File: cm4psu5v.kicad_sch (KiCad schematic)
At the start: 26 parts, among them U13 AP64501SP-13

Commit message: respin
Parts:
- renumbered C46 to C48, C47 to C49, C48 to C50, C49 to C51, C50 to C52, C51 to C53, C52 to C54, C53 to C55, C54 to C56, C55 to C57, C56 to C58, C57 to C59, C58 to C60, C59 to C61, C60 to C62, C61 to C63, D10 to D9, R39 to R42, R40 to R43, R41 to R44, R42 to R45, R43 to R46, U13 to U14
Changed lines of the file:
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@@
   (symbol (lib_id "power:GND") (at 152.4 148.59 0) (unit 1)
     (in_bom yes) (on_board yes)
-    (property "Reference" "#PWR043" (id 0) (at 152.4 154.94 0)
+    (property "Reference" "#PWR044" (id 0) (at 152.4 154.94 0)
       (effects (font (size 1.27 1.27)) hide)
     )
@@
   (symbol (lib_id "Device:C_Small") (at 259.08 111.76 0) (unit 1)
     (in_bom yes) (on_board yes)
-    (property "Reference" "C58" (id 0) (at 261.62 110.49 0)
+    (property "Reference" "C60" (id 0) (at 261.62 110.49 0)
       (effects (font (size 1.27 1.27)) (justify left))
     )
@@
   (symbol (lib_id "Device:R_Small") (at 226.06 137.16 0) (unit 1)
     (in_bom yes) (on_board yes)
-    (property "Reference" "R42" (id 0) (at 227.33 135.89 0)
+    (property "Reference" "R45" (id 0) (at 227.33 135.89 0)
       (effects (font (size 1.27 1.27)) (justify left))
     )
@@
   (symbol (lib_id "Device:R_Small") (at 219.71 118.11 0) (unit 1)
     (in_bom yes) (on_board yes)
-    (property "Reference" "R41" (id 0) (at 220.98 116.84 0)
+    (property "Reference" "R44" (id 0) (at 220.98 116.84 0)
       (effects (font (size 1.27 1.27)) (justify left))
     )
@@
   (symbol (lib_id "Device:C_Small") (at 232.41 118.11 0) (unit 1)
     (in_bom no) (on_board no)
-    (property "Reference" "C56" (id 0) (at 234.95 116.84 0)
+    (property "Reference" "C58" (id 0) (at 234.95 116.84 0)
       (effects (font (size 1.27 1.27)) (justify left))
     )
@@
   (symbol (lib_id "Device:C_Small") (at 213.36 140.97 0) (unit 1)
     (in_bom yes) (on_board yes)
-    (property "Reference" "C55" (id 0) (at 215.9 139.7 0)
+    (property "Reference" "C57" (id 0) (at 215.9 139.7 0)
       (effects (font (size 1.27 1.27)) (justify left))
     )
@@
   (symbol (lib_id "Device:R_Small") (at 306.705 112.395 0) (unit 1)
     (in_bom yes) (on_board yes)
-    (property "Reference" "R43" (id 0) (at 309.88 111.125 0))
+    (property "Reference" "R46" (id 0) (at 309.88 111.125 0))
     (property "Value" "1k" (id 1) (at 309.88 113.665 0))
     (property "Footprint" "Resistor_SMD:R_0402_1005Metric" (id 2) (at 306.705 112.395 0)
@@
   (symbol (lib_id "power:GND") (at 290.83 148.59 0) (unit 1)
     (in_bom yes) (on_board yes)
-    (property "Reference" "#PWR047" (id 0) (at 290.83 154.94 0)
+    (property "Reference" "#PWR048" (id 0) (at 290.83 154.94 0)
       (effects (font (size 1.27 1.27)) hide)
     )
@@
   (symbol (lib_id "Regulator_Switching_Diodes:AP64501SP-13") (at 182.88 124.46 0) (unit 1)
     (in_bom yes) (on_board yes)
-    (property "Reference" "U13" (id 0) (at 182.245 114.3 0))
+    (property "Reference" "U14" (id 0) (at 182.245 114.3 0))
     (property "Value" "AP64501SP-13" (id 1) (at 182.88 116.84 0))
     (property "Footprint" "Regulator_Switching_Diodes:SOIC-8-1EP_3.9x4.9mm_P1.27mm_EP2.95x4.9mm_Mask2.71x3.4mm_ThermalVias" (id 2) (at 182.88 149.86 0)
@@
   (symbol (lib_id "Device:C_Small") (at 248.92 111.76 0) (unit 1)
     (in_bom yes) (on_board yes)
-    (property "Reference" "C57" (id 0) (at 251.46 110.49 0)
+    (property "Reference" "C59" (id 0) (at 251.46 110.49 0)
       (effects (font (size 1.27 1.27)) (justify left))
     )
@@
   (symbol (lib_id "power:GND") (at 279.4 148.59 0) (unit 1)
     (in_bom yes) (on_board yes)
-    (property "Reference" "#PWR046" (id 0) (at 279.4 154.94 0)
+    (property "Reference" "#PWR047" (id 0) (at 279.4 154.94 0)
       (effects (font (size 1.27 1.27)) hide)
     )
@@
   (symbol (lib_id "Device:C_Small") (at 163.83 114.3 0) (unit 1)
     (in_bom yes) (on_board yes)
-    (property "Reference" "C52" (id 0) (at 166.37 113.03 0)
+    (property "Reference" "C54" (id 0) (at 166.37 113.03 0)
       (effects (font (size 1.27 1.27)) (justify left))
     )
@@
   (symbol (lib_id "Device:R_Small") (at 173.99 106.68 270) (unit 1)
     (in_bom yes) (on_board yes)
-    (property "Reference" "R39" (id 0) (at 172.72 104.14 90)
+    (property "Reference" "R42" (id 0) (at 172.72 104.14 90)
       (effects (font (size 1.27 1.27)) (justify left))
     )
@@
   (symbol (lib_id "Device:R_Small") (at 213.36 133.35 0) (unit 1)
     (in_bom yes) (on_board yes)
-    (property "Reference" "R40" (id 0) (at 215.9 132.08 0)
+    (property "Reference" "R43" (id 0) (at 215.9 132.08 0)
       (effects (font (size 1.27 1.27)) (justify left))
     )
@@
   (symbol (lib_id "Device:C_Small") (at 279.4 111.76 0) (unit 1)
     (in_bom yes) (on_board yes)
-    (property "Reference" "C60" (id 0) (at 281.94 110.49 0)
+    (property "Reference" "C62" (id 0) (at 281.94 110.49 0)
       (effects (font (size 1.27 1.27)) (justify left))
     )
@@
   (symbol (lib_id "Device:C_Small") (at 172.72 137.16 0) (unit 1)
     (in_bom yes) (on_board yes)
-    (property "Reference" "C53" (id 0) (at 175.26 135.89 0)
+    (property "Reference" "C55" (id 0) (at 175.26 135.89 0)
       (effects (font (size 1.27 1.27)) (justify left))
     )
@@
   (symbol (lib_id "power:GND") (at 226.06 148.59 0) (unit 1)
     (in_bom yes) (on_board yes)
-    (property "Reference" "#PWR044" (id 0) (at 226.06 154.94 0)
+    (property "Reference" "#PWR045" (id 0) (at 226.06 154.94 0)
       (effects (font (size 1.27 1.27)) hide)
     )
@@
   (symbol (lib_id "Device:C_Small") (at 152.4 128.27 0) (unit 1)
     (in_bom yes) (on_board yes)
-    (property "Reference" "C51" (id 0) (at 154.94 127 0)
+    (property "Reference" "C53" (id 0) (at 154.94 127 0)
       (effects (font (size 1.27 1.27)) (justify left))
     )
@@
   (symbol (lib_id "Device:C_Small") (at 91.44 128.27 0) (unit 1)
     (in_bom yes) (on_board yes)
-    (property "Reference" "C47" (id 0) (at 93.98 127 0)
+    (property "Reference" "C49" (id 0) (at 93.98 127 0)
       (effects (font (size 1.27 1.27)) (justify left))
     )
@@
   (symbol (lib_id "Device:C_Small") (at 269.24 111.76 0) (unit 1)
     (in_bom yes) (on_board yes)
-    (property "Reference" "C59" (id 0) (at 271.78 110.49 0)
+    (property "Reference" "C61" (id 0) (at 271.78 110.49 0)
       (effects (font (size 1.27 1.27)) (justify left))
     )
@@
   (symbol (lib_id "power:GND") (at 306.705 148.59 0) (unit 1)
     (in_bom yes) (on_board yes)
-    (property "Reference" "#PWR048" (id 0) (at 306.705 154.94 0)
+    (property "Reference" "#PWR049" (id 0) (at 306.705 154.94 0)
       (effects (font (size 1.27 1.27)) hide)
     )
@@
   (symbol (lib_id "Device:C_Small") (at 76.2 128.27 0) (unit 1)
     (in_bom yes) (on_board yes)
-    (property "Reference" "C46" (id 0) (at 78.74 127 0)
+    (property "Reference" "C48" (id 0) (at 78.74 127 0)
       (effects (font (size 1.27 1.27)) (justify left))
     )
@@
   (symbol (lib_id "power:GND") (at 251.46 142.24 0) (unit 1)
     (in_bom yes) (on_board yes)
-    (property "Reference" "#PWR045" (id 0) (at 251.46 148.59 0)
+    (property "Reference" "#PWR046" (id 0) (at 251.46 148.59 0)
       (effects (font (size 1.27 1.27)) hide)
     )
@@
   (symbol (lib_id "Capacitor_Tantalum_SMD_MyOwn:CP_EIA-7343-31_Kemet-D") (at 290.83 111.76 0) (unit 1)
     (in_bom yes) (on_board yes)
-    (property "Reference" "C61" (id 0) (at 293.37 110.49 0)
+    (property "Reference" "C63" (id 0) (at 293.37 110.49 0)
       (effects (font (size 1.27 1.27)) (justify left))
     )
@@
   (symbol (lib_id "Device:C_Small") (at 121.92 128.27 0) (unit 1)
     (in_bom yes) (on_board yes)
-    (property "Reference" "C49" (id 0) (at 124.46 127 0)
+    (property "Reference" "C51" (id 0) (at 124.46 127 0)
       (effects (font (size 1.27 1.27)) (justify left))
     )
@@
   (symbol (lib_id "Device:C_Small") (at 106.68 128.27 0) (unit 1)
     (in_bom yes) (on_board yes)
-    (property "Reference" "C48" (id 0) (at 109.22 127 0)
+    (property "Reference" "C50" (id 0) (at 109.22 127 0)
       (effects (font (size 1.27 1.27)) (justify left))
     )
@@
   (symbol (lib_id "Device:C_Small") (at 137.16 128.27 0) (unit 1)
     (in_bom yes) (on_board yes)
-    (property "Reference" "C50" (id 0) (at 139.7 127 0)
+    (property "Reference" "C52" (id 0) (at 139.7 127 0)
       (effects (font (size 1.27 1.27)) (justify left))
     )
@@
   (symbol (lib_id "Device:C_Small") (at 201.93 137.16 0) (unit 1)
     (in_bom yes) (on_board yes)
-    (property "Reference" "C54" (id 0) (at 204.47 135.89 0)
+    (property "Reference" "C56" (id 0) (at 204.47 135.89 0)
       (effects (font (size 1.27 1.27)) (justify left))
     )
@@
   (symbol (lib_id "LED_SMD_LiteOn:LED Green") (at 306.705 121.285 270) (unit 1)
     (in_bom yes) (on_board yes)
-    (property "Reference" "D10" (id 0) (at 309.88 120.65 90))
+    (property "Reference" "D9" (id 0) (at 309.88 120.65 90))
     (property "Value" "LED Green" (id 1) (at 313.69 122.555 90))
     (property "Footprint" "LED_SMD_LiteOn:LED_0603_1608Metric_green" (id 2) (at 296.545 121.285 0)

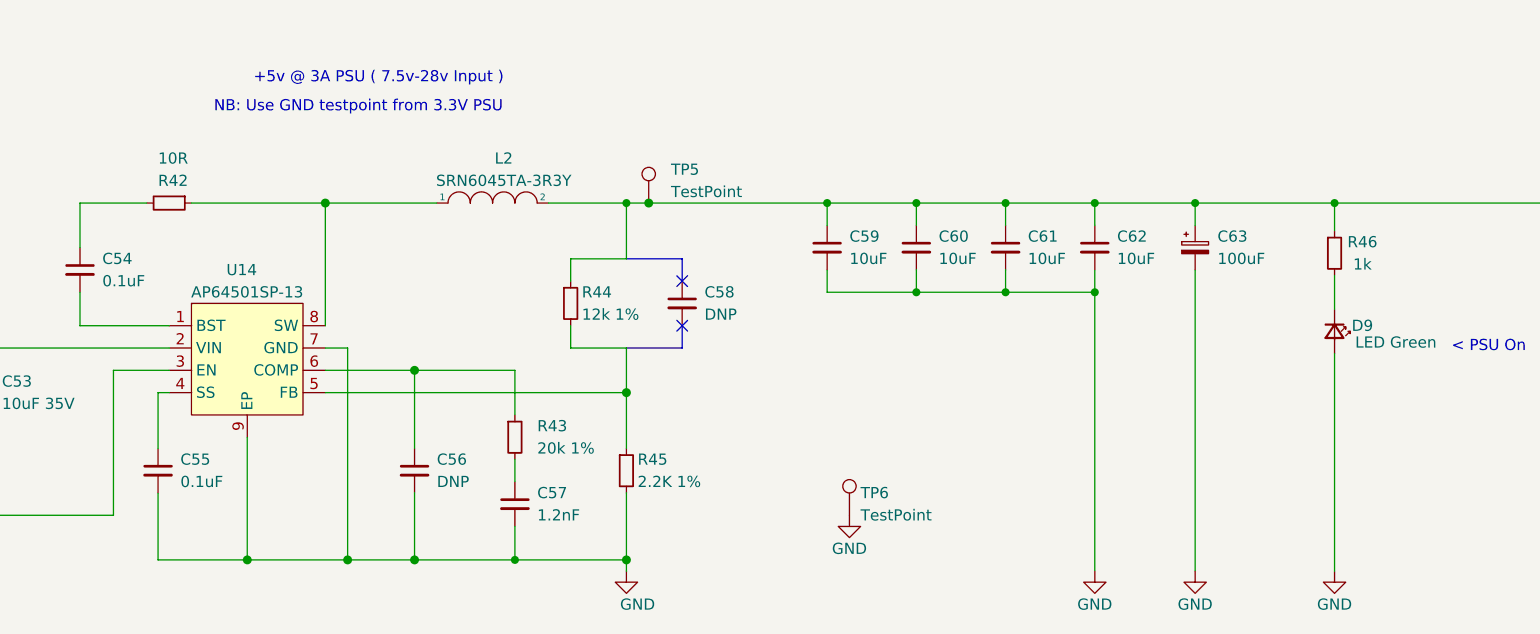
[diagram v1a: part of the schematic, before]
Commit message: fixed I2C ping indicator
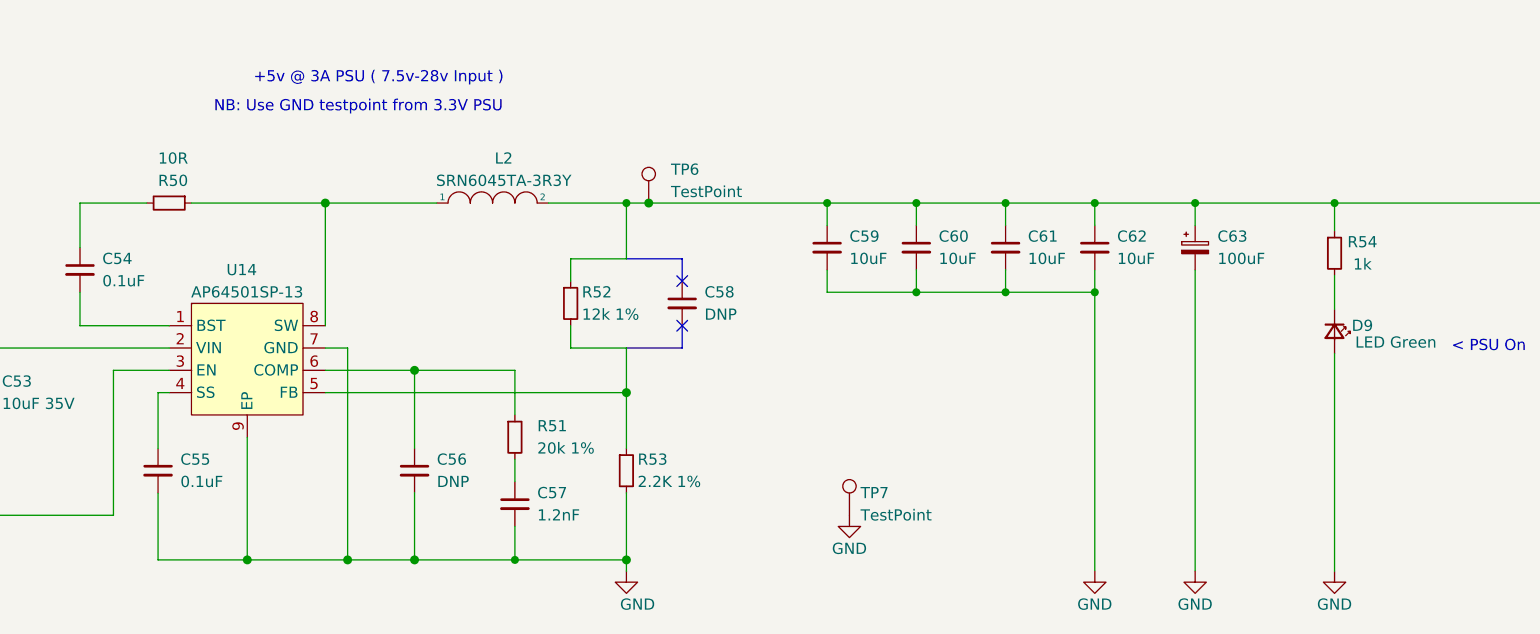
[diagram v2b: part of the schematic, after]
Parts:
- renumbered R42 to R50, R43 to R51, R44 to R52, R45 to R53, R46 to R54, TP5 to TP6, TP6 to TP7
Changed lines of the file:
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@@
   (symbol (lib_id "power:GND") (at 152.4 148.59 0) (unit 1)
     (in_bom yes) (on_board yes)
-    (property "Reference" "#PWR044" (id 0) (at 152.4 154.94 0)
+    (property "Reference" "#PWR046" (id 0) (at 152.4 154.94 0)
       (effects (font (size 1.27 1.27)) hide)
     )
@@
   (symbol (lib_id "Device:R_Small") (at 226.06 137.16 0) (unit 1)
     (in_bom yes) (on_board yes)
-    (property "Reference" "R45" (id 0) (at 227.33 135.89 0)
+    (property "Reference" "R53" (id 0) (at 227.33 135.89 0)
       (effects (font (size 1.27 1.27)) (justify left))
     )
@@
   (symbol (lib_id "Device:R_Small") (at 219.71 118.11 0) (unit 1)
     (in_bom yes) (on_board yes)
-    (property "Reference" "R44" (id 0) (at 220.98 116.84 0)
+    (property "Reference" "R52" (id 0) (at 220.98 116.84 0)
       (effects (font (size 1.27 1.27)) (justify left))
     )
@@
   (symbol (lib_id "Connector:TestPoint") (at 251.46 142.24 0) (unit 1)
     (in_bom yes) (on_board yes)
-    (property "Reference" "TP6" (id 0) (at 252.73 139.7 0)
+    (property "Reference" "TP7" (id 0) (at 252.73 139.7 0)
       (effects (font (size 1.27 1.27)) (justify left))
     )
@@
   (symbol (lib_id "Device:R_Small") (at 306.705 112.395 0) (unit 1)
     (in_bom yes) (on_board yes)
-    (property "Reference" "R46" (id 0) (at 309.88 111.125 0))
+    (property "Reference" "R54" (id 0) (at 309.88 111.125 0))
     (property "Value" "1k" (id 1) (at 309.88 113.665 0))
     (property "Footprint" "Resistor_SMD:R_0402_1005Metric" (id 2) (at 306.705 112.395 0)
@@
   (symbol (lib_id "power:GND") (at 290.83 148.59 0) (unit 1)
     (in_bom yes) (on_board yes)
-    (property "Reference" "#PWR048" (id 0) (at 290.83 154.94 0)
+    (property "Reference" "#PWR050" (id 0) (at 290.83 154.94 0)
       (effects (font (size 1.27 1.27)) hide)
     )
@@
   (symbol (lib_id "power:GND") (at 279.4 148.59 0) (unit 1)
     (in_bom yes) (on_board yes)
-    (property "Reference" "#PWR047" (id 0) (at 279.4 154.94 0)
+    (property "Reference" "#PWR049" (id 0) (at 279.4 154.94 0)
       (effects (font (size 1.27 1.27)) hide)
     )
@@
   (symbol (lib_id "Device:R_Small") (at 173.99 106.68 270) (unit 1)
     (in_bom yes) (on_board yes)
-    (property "Reference" "R42" (id 0) (at 172.72 104.14 90)
+    (property "Reference" "R50" (id 0) (at 172.72 104.14 90)
       (effects (font (size 1.27 1.27)) (justify left))
     )
@@
   (symbol (lib_id "Device:R_Small") (at 213.36 133.35 0) (unit 1)
     (in_bom yes) (on_board yes)
-    (property "Reference" "R43" (id 0) (at 215.9 132.08 0)
+    (property "Reference" "R51" (id 0) (at 215.9 132.08 0)
       (effects (font (size 1.27 1.27)) (justify left))
     )
@@
   (symbol (lib_id "Connector:TestPoint") (at 228.6 106.68 0) (unit 1)
     (in_bom yes) (on_board yes)
-    (property "Reference" "TP5" (id 0) (at 231.14 102.87 0)
+    (property "Reference" "TP6" (id 0) (at 231.14 102.87 0)
       (effects (font (size 1.27 1.27)) (justify left))
     )
@@
   (symbol (lib_id "power:GND") (at 226.06 148.59 0) (unit 1)
     (in_bom yes) (on_board yes)
-    (property "Reference" "#PWR045" (id 0) (at 226.06 154.94 0)
+    (property "Reference" "#PWR047" (id 0) (at 226.06 154.94 0)
       (effects (font (size 1.27 1.27)) hide)
     )
@@
   (symbol (lib_id "power:GND") (at 306.705 148.59 0) (unit 1)
     (in_bom yes) (on_board yes)
-    (property "Reference" "#PWR049" (id 0) (at 306.705 154.94 0)
+    (property "Reference" "#PWR051" (id 0) (at 306.705 154.94 0)
       (effects (font (size 1.27 1.27)) hide)
     )
@@
   (symbol (lib_id "power:GND") (at 251.46 142.24 0) (unit 1)
     (in_bom yes) (on_board yes)
-    (property "Reference" "#PWR046" (id 0) (at 251.46 148.59 0)
-      (effects (font (size 1.27 1.27)) hide)
-    )
+    (property "Reference" "#PWR048" (id 0) (at 251.46 148.59 0)
+      (effects (font (size 1.27 1.27)) hide)
+    )

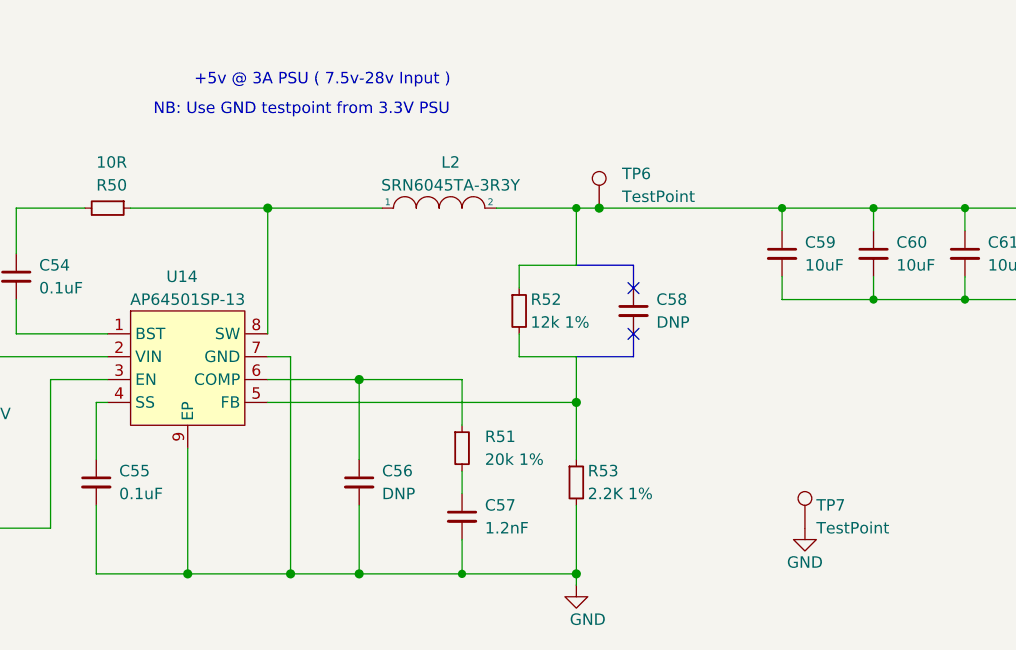
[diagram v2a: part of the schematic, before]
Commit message: added ti buffer lib
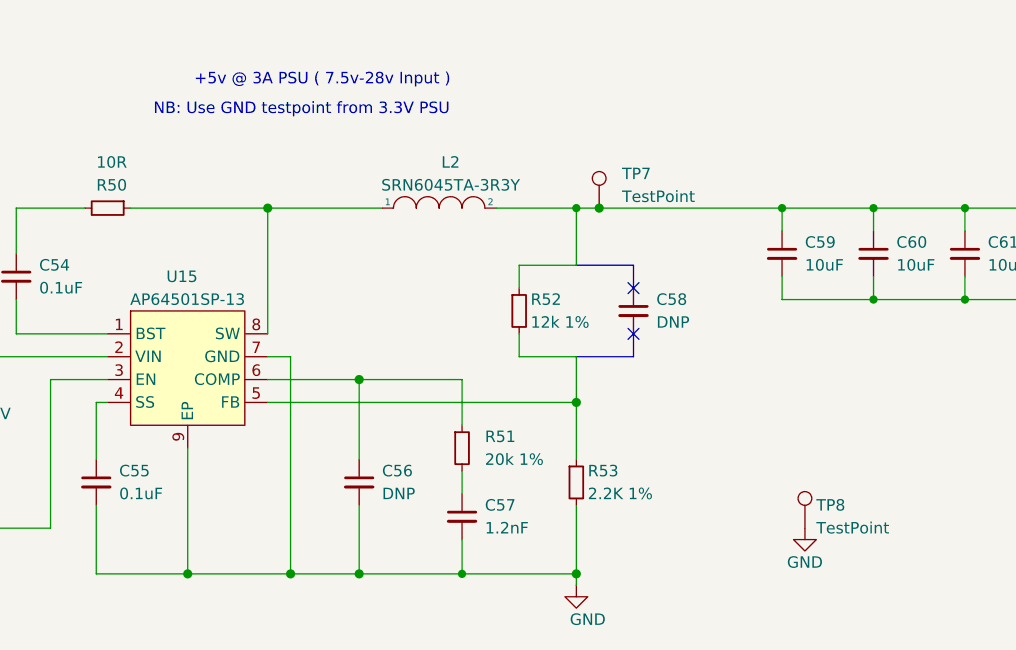
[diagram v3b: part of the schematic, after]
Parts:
- renumbered TP6 to TP7, TP7 to TP8, U14 to U15
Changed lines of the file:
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@@
   (symbol (lib_id "power:GND") (at 152.4 148.59 0) (unit 1)
     (in_bom yes) (on_board yes)
-    (property "Reference" "#PWR046" (id 0) (at 152.4 154.94 0)
+    (property "Reference" "#PWR048" (id 0) (at 152.4 154.94 0)
       (effects (font (size 1.27 1.27)) hide)
     )
@@
   (symbol (lib_id "Connector:TestPoint") (at 251.46 142.24 0) (unit 1)
     (in_bom yes) (on_board yes)
-    (property "Reference" "TP7" (id 0) (at 252.73 139.7 0)
+    (property "Reference" "TP8" (id 0) (at 252.73 139.7 0)
       (effects (font (size 1.27 1.27)) (justify left))
     )
@@
   (symbol (lib_id "power:GND") (at 290.83 148.59 0) (unit 1)
     (in_bom yes) (on_board yes)
-    (property "Reference" "#PWR050" (id 0) (at 290.83 154.94 0)
+    (property "Reference" "#PWR052" (id 0) (at 290.83 154.94 0)
       (effects (font (size 1.27 1.27)) hide)
     )
@@
   (symbol (lib_id "Regulator_Switching_Diodes:AP64501SP-13") (at 182.88 124.46 0) (unit 1)
     (in_bom yes) (on_board yes)
-    (property "Reference" "U14" (id 0) (at 182.245 114.3 0))
+    (property "Reference" "U15" (id 0) (at 182.245 114.3 0))
     (property "Value" "AP64501SP-13" (id 1) (at 182.88 116.84 0))
     (property "Footprint" "Regulator_Switching_Diodes:SOIC-8-1EP_3.9x4.9mm_P1.27mm_EP2.95x4.9mm_Mask2.71x3.4mm_ThermalVias" (id 2) (at 182.88 149.86 0)
@@
   (symbol (lib_id "power:GND") (at 279.4 148.59 0) (unit 1)
     (in_bom yes) (on_board yes)
-    (property "Reference" "#PWR049" (id 0) (at 279.4 154.94 0)
+    (property "Reference" "#PWR051" (id 0) (at 279.4 154.94 0)
       (effects (font (size 1.27 1.27)) hide)
     )
@@
   (symbol (lib_id "Connector:TestPoint") (at 228.6 106.68 0) (unit 1)
     (in_bom yes) (on_board yes)
-    (property "Reference" "TP6" (id 0) (at 231.14 102.87 0)
+    (property "Reference" "TP7" (id 0) (at 231.14 102.87 0)
       (effects (font (size 1.27 1.27)) (justify left))
     )
@@
   (symbol (lib_id "power:GND") (at 226.06 148.59 0) (unit 1)
     (in_bom yes) (on_board yes)
-    (property "Reference" "#PWR047" (id 0) (at 226.06 154.94 0)
+    (property "Reference" "#PWR049" (id 0) (at 226.06 154.94 0)
       (effects (font (size 1.27 1.27)) hide)
     )
@@
   (symbol (lib_id "power:GND") (at 306.705 148.59 0) (unit 1)
     (in_bom yes) (on_board yes)
-    (property "Reference" "#PWR051" (id 0) (at 306.705 154.94 0)
+    (property "Reference" "#PWR053" (id 0) (at 306.705 154.94 0)
       (effects (font (size 1.27 1.27)) hide)
     )
@@
   (symbol (lib_id "power:GND") (at 251.46 142.24 0) (unit 1)
     (in_bom yes) (on_board yes)
-    (property "Reference" "#PWR048" (id 0) (at 251.46 148.59 0)
-      (effects (font (size 1.27 1.27)) hide)
-    )
+    (property "Reference" "#PWR050" (id 0) (at 251.46 148.59 0)
+      (effects (font (size 1.27 1.27)) hide)
+    )
